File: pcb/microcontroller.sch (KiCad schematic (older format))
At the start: 14 parts, among them J1 JSTA-4, P2 SWD, SW1 SPST, U2 STM32F072CBT6

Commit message: Generated net list (only two footprints remaining), added a few footprints, started rough estimate of PCB size
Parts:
- D401: renamed from D2; footprint (none) -> Woodchuck:CREE_RGB_LED; Farnell (none) -> 2093940
- gave numbers to parts that had none: 1
- renumbered C5 to C401, C6 to C402, C7 to C403, C8 to C404, J1 to J401, P2 to P401, R2 to R401, R3 to R402, R4 to R403, R1 to R404, SW1 to SW401, U2 to U401
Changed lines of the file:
@@
 $EndDescr
 $Comp
-L GND #PWR24
+L GND #PWR017
 U 1 1 565B23CF
 P 5900 5600
-F 0 "#PWR24" H 5900 5350 50  0001 C CNN
+F 0 "#PWR017" H 5900 5350 50  0001 C CNN
 F 1 "GND" H 5900 5450 50  0000 C CNN
 F 2 "" H 5900 5600 60  0000 C CNN
@@
 $EndComp
 $Comp
-L C C7
+L C C403
 U 1 1 565B2484
 P 3000 2000
-F 0 "C7" H 3025 2100 50  0000 L CNN
+F 0 "C403" H 3025 2100 50  0000 L CNN
 F 1 "0.1uF" H 3025 1900 50  0000 L CNN
 F 2 "Woodchuck:C0603" H 3038 1850 30  0000 C CNN
@@
 $EndComp
 $Comp
-L GND #PWR21
+L GND #PWR018
 U 1 1 565B2D06
 P 3000 2350
-F 0 "#PWR21" H 3000 2100 50  0001 C CNN
+F 0 "#PWR018" H 3000 2100 50  0001 C CNN
 F 1 "GND" H 3000 2200 50  0000 C CNN
 F 2 "" H 3000 2350 60  0000 C CNN
@@
 $EndComp
 $Comp
-L C C6
+L C C402
 U 1 1 565B2D3B
 P 2750 2000
-F 0 "C6" H 2775 2100 50  0000 L CNN
+F 0 "C402" H 2775 2100 50  0000 L CNN
 F 1 "0.1uF" H 2775 1900 50  0000 L CNN
 F 2 "Woodchuck:C0603" H 2788 1850 30  0000 C CNN
@@
 NOTE: Place one near each\nVDD pin (24, 48) and one\nnear VDDIO2 (36)
 $Comp
-L C C5
+L C C401
 U 1 1 565B339D
 P 1650 2000
-F 0 "C5" H 1675 2100 50  0000 L CNN
+F 0 "C401" H 1675 2100 50  0000 L CNN
 F 1 "10nF" H 1675 1900 50  0000 L CNN
 F 2 "Woodchuck:C0603" H 1688 1850 30  0000 C CNN
@@
 $EndComp
 $Comp
-L GND #PWR13
+L GND #PWR019
 U 1 1 565B33AB
 P 1650 2250
-F 0 "#PWR13" H 1650 2000 50  0001 C CNN
+F 0 "#PWR019" H 1650 2000 50  0001 C CNN
 F 1 "GND" H 1650 2100 50  0000 C CNN
 F 2 "" H 1650 2250 60  0000 C CNN
@@
 NOTE: Place near VDDA (9)
 $Comp
-L C C8
+L C C404
 U 1 1 565B3429
 P 3250 2000
-F 0 "C8" H 3275 2100 50  0000 L CNN
+F 0 "C404" H 3275 2100 50  0000 L CNN
 F 1 "0.1uF" H 3275 1900 50  0000 L CNN
 F 2 "Woodchuck:C0603" H 3288 1850 30  0000 C CNN
@@
 NOTE: VDD supply needs 4.7uF across it
 $Comp
-L SWD P2
+L SWD P401
 U 1 1 565B3F04
 P 2300 3450
-F 0 "P2" H 2550 3750 60  0000 C CNN
+F 0 "P401" H 2550 3750 60  0000 C CNN
 F 1 "SWD" H 2000 3750 60  0000 C CNN
 F 2 "Woodchuck:FTSH-105-01-F-D-K" H 2650 3250 60  0001 C CNN
@@
 SWCLK
 $Comp
-L GND #PWR15
+L GND #PWR020
 U 1 1 565B4620
 P 1700 3750
-F 0 "#PWR15" H 1700 3500 50  0001 C CNN
+F 0 "#PWR020" H 1700 3500 50  0001 C CNN
 F 1 "GND" H 1700 3600 50  0000 C CNN
 F 2 "" H 1700 3750 60  0000 C CNN
@@
 $EndComp
 $Comp
-L JSTA-4 J1
+L JSTA-4 J401
 U 1 1 565B5A63
 P 2500 4550
-F 0 "J1" H 2550 4100 60  0000 C CNN
+F 0 "J401" H 2550 4100 60  0000 C CNN
 F 1 "JSTA-4" H 2500 4600 60  0000 C CNN
 F 2 "Woodchuck:S04B-PASK-2" H 2500 4650 60  0001 C CNN
@@
 EXT_RX
 $Comp
-L GND #PWR17
+L GND #PWR021
 U 1 1 565B6C28
 P 2200 5000
-F 0 "#PWR17" H 2200 4750 50  0001 C CNN
+F 0 "#PWR021" H 2200 4750 50  0001 C CNN
 F 1 "GND" H 2200 4850 50  0000 C CNN
 F 2 "" H 2200 5000 60  0000 C CNN
@@
 EXT PORT
 $Comp
-L GND #PWR18
+L GND #PWR022
 U 1 1 565B80EF
 P 2400 6100
-F 0 "#PWR18" H 2400 5850 50  0001 C CNN
+F 0 "#PWR022" H 2400 5850 50  0001 C CNN
 F 1 "GND" H 2400 5950 50  0000 C CNN
 F 2 "" H 2400 6100 60  0000 C CNN
@@
 $EndComp
 $Comp
-L GND #PWR19
+L GND #PWR023
 U 1 1 565B8112
 P 2800 6300
-F 0 "#PWR19" H 2800 6050 50  0001 C CNN
+F 0 "#PWR023" H 2800 6050 50  0001 C CNN
 F 1 "GND" H 2800 6150 50  0000 C CNN
 F 2 "" H 2800 6300 60  0000 C CNN
@@
 BOOT0
 $Comp
-L SPST SW1
+L SPST SW401
 U 1 1 565B9D59
 P 8550 4750
-F 0 "SW1" H 8550 4850 50  0000 C CNN
+F 0 "SW401" H 8550 4850 50  0000 C CNN
 F 1 "SPST" H 8550 4650 50  0000 C CNN
 F 2 "" H 8550 4750 60  0000 C CNN
@@
 BOOT0
 $Comp
-L RESISTOR R1
+L RESISTOR R404
 U 1 1 565BA71B
 P 7950 5100
-F 0 "R1" H 8070 5190 60  0000 C CNN
+F 0 "R404" H 8070 5190 60  0000 C CNN
 F 1 "10K" H 7950 4950 60  0000 C CNN
 F 2 "Woodchuck:0603" H 7950 4850 60  0000 C CNN
@@
 $EndComp
 $Comp
-L GND #PWR25
+L GND #PWR024
 U 1 1 565BAC22
 P 7950 5450
-F 0 "#PWR25" H 7950 5200 50  0001 C CNN
+F 0 "#PWR024" H 7950 5200 50  0001 C CNN
 F 1 "GND" H 7950 5300 50  0000 C CNN
 F 2 "" H 7950 5450 60  0000 C CNN
@@
 BOOTLOADER SELECT
 $Comp
-L +3.3V #PWR26
+L +3.3V #PWR025
 U 1 1 565F343F
 P 9150 4650
-F 0 "#PWR26" H 9150 4500 50  0001 C CNN
+F 0 "#PWR025" H 9150 4500 50  0001 C CNN
 F 1 "+3.3V" H 9150 4790 50  0000 C CNN
 F 2 "" H 9150 4650 50  0000 C CNN
@@
 $EndComp
 $Comp
-L +3.3V #PWR16
+L +3.3V #PWR026
 U 1 1 565F3C95
 P 2200 4500
-F 0 "#PWR16" H 2200 4350 50  0001 C CNN
+F 0 "#PWR026" H 2200 4350 50  0001 C CNN
 F 1 "+3.3V" H 2200 4640 50  0000 C CNN
 F 2 "" H 2200 4500 50  0000 C CNN
@@
 $EndComp
 $Comp
-L +3.3V #PWR14
+L +3.3V #PWR027
 U 1 1 565F3F3F
 P 1700 3150
-F 0 "#PWR14" H 1700 3000 50  0001 C CNN
+F 0 "#PWR027" H 1700 3000 50  0001 C CNN
 F 1 "+3.3V" H 1700 3290 50  0000 C CNN
 F 2 "" H 1700 3150 50  0000 C CNN
@@
 $EndComp
 $Comp
-L +3.3V #PWR20
+L +3.3V #PWR028
 U 1 1 565F40A9
 P 3000 1650
-F 0 "#PWR20" H 3000 1500 50  0001 C CNN
+F 0 "#PWR028" H 3000 1500 50  0001 C CNN
 F 1 "+3.3V" H 3000 1790 50  0000 C CNN
 F 2 "" H 3000 1650 50  0000 C CNN
@@
 $EndComp
 $Comp
-L +3.3V #PWR12
+L +3.3V #PWR029
 U 1 1 565F40DC
 P 1650 1750
-F 0 "#PWR12" H 1650 1600 50  0001 C CNN
+F 0 "#PWR029" H 1650 1600 50  0001 C CNN
 F 1 "+3.3V" H 1650 1890 50  0000 C CNN
 F 2 "" H 1650 1750 50  0000 C CNN
@@
 $EndComp
 $Comp
-L +3.3V #PWR23
+L +3.3V #PWR030
 U 1 1 565F4A36
 P 5800 2400
-F 0 "#PWR23" H 5800 2250 50  0001 C CNN
+F 0 "#PWR030" H 5800 2250 50  0001 C CNN
 F 1 "+3.3V" H 5800 2540 50  0000 C CNN
 F 2 "" H 5800 2400 50  0000 C CNN
@@
 NoConn ~ 5500 2600
 $Comp
-L LED_RCBG D2
+L LED_RCBG D401
 U 1 1 569D292A
 P 3700 4500
-F 0 "D2" H 3700 4850 50  0000 C CNN
+F 0 "D401" H 3700 4850 50  0000 C CNN
 F 1 "LED_RCBG" H 3700 4150 50  0000 C CNN
-F 2 "" H 3700 4450 50  0000 C CNN
-F 3 "" H 3700 4450 50  0000 C CNN
+F 2 "Woodchuck:CREE_RGB_LED" H 3650 5000 50  0000 C CNN
+F 3 "http://www.farnell.com/datasheets/1965387.pdf" H 3600 4900 50  0000 C CNN
+F 4 "2093940" H 3700 4500 60  0001 C CNN "Farnell"
 	1    3700 4500
 	0    -1   -1   0
 $EndComp
 $Comp
-L RESISTOR R2
+L RESISTOR R401
 U 1 1 569D2BC0
 P 4500 4000
-F 0 "R2" H 4620 4090 60  0000 C CNN
+F 0 "R401" H 4620 4090 60  0000 C CNN
 F 1 "RESISTOR" H 4500 3850 60  0001 C CNN
 F 2 "Woodchuck:0603" H 4500 4000 60  0001 C CNN
@@
 $EndComp
 $Comp
-L RESISTOR R3
+L RESISTOR R402
 U 1 1 569D2C37
 P 4500 4100
-F 0 "R3" H 4620 4190 60  0000 C CNN
+F 0 "R402" H 4620 4190 60  0000 C CNN
 F 1 "RESISTOR" H 4500 3950 60  0001 C CNN
 F 2 "Woodchuck:0603" H 4500 4100 60  0001 C CNN
@@
 $EndComp
 $Comp
-L RESISTOR R4
+L RESISTOR R403
 U 1 1 569D2C6E
 P 4500 4200
-F 0 "R4" H 4620 4290 60  0000 C CNN
+F 0 "R403" H 4620 4290 60  0000 C CNN
 F 1 "RESISTOR" H 4500 4050 60  0001 C CNN
 F 2 "Woodchuck:0603" H 4500 4200 60  0001 C CNN
@@
 $EndComp
 $Comp
-L STM32F072CBT6 U2
+L STM32F072CBT6 U401
 U 1 1 565B237E
 P 5050 2800
-F 0 "U2" H 5100 2850 60  0000 C CNN
+F 0 "U401" H 5100 2850 60  0000 C CNN
 F 1 "STM32F072CBT6" H 6300 2850 60  0000 C CNN
 F 2 "Woodchuck:LQFP48" H 5400 2900 60  0001 C CNN
@@
 $EndComp
 $Comp
-L GND #PWR22
+L GND #PWR031
 U 1 1 569D2FC5
 P 3700 4850
-F 0 "#PWR22" H 3700 4600 50  0001 C CNN
+F 0 "#PWR031" H 3700 4600 50  0001 C CNN
 F 1 "GND" H 3700 4700 50  0000 C CNN
 F 2 "" H 3700 4850 60  0000 C CNN
@@
 $EndComp
 $Comp
-L USB_OTG P?
+L USB_OTG P402
 U 1 1 569D56C3
 P 2700 5850
-F 0 "P?" H 3025 5725 50  0000 C CNN
+F 0 "P402" H 3025 5725 50  0000 C CNN
 F 1 "USB_OTG" H 2700 6050 50  0000 C CNN
 F 2 "Woodchuck:MOLEX_67503_1020_MINI_USB" V 2650 5750 60  0001 C CNN

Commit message: Fix LED circuit and radio tx/rx labels, start LED driver code
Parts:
- D401: value LED_RCBG -> LED_RABG; symbol LED_RCBG -> LED_RABG; Digikey (none) -> Value; Fieldname (none) -> Value
- R401, R402, R403: value RESISTOR -> 510; Farnell Value -> 1469826
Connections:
- wire segments 69 -> 70
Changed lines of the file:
@@
 NoConn ~ 5500 2600
 $Comp
-L LED_RCBG D401
+L LED_RABG D401
 U 1 1 569D292A
-P 3700 4500
-F 0 "D401" H 3700 4850 50  0000 C CNN
-F 1 "LED_RCBG" H 3700 4150 50  0000 C CNN
-F 2 "Woodchuck:CREE_RGB_LED" H 3650 5000 50  0000 C CNN
-F 3 "http://www.farnell.com/datasheets/1965387.pdf" H 3600 4900 50  0000 C CNN
-F 4 "2093940" H 3700 4500 60  0001 C CNN "Farnell"
-	1    3700 4500
+P 3700 3550
+F 0 "D401" H 3700 3900 50  0000 C CNN
+F 1 "LED_RABG" H 3700 3200 50  0001 C CNN
+F 2 "Woodchuck:CREE_RGB_LED" H 3650 4050 50  0001 C CNN
+F 3 "http://www.farnell.com/datasheets/1965387.pdf" H 3600 3950 50  0001 C CNN
+F 4 "Value" H 3700 3550 60  0001 C CNN "Digikey"
+F 5 "2093940" H 3700 3550 60  0001 C CNN "Farnell"
+F 6 "Value" H 3700 3550 60  0001 C CNN "Fieldname"
+	1    3700 3550
 	0    -1   -1   0
 $EndComp
@@
 P 4500 4000
 F 0 "R401" H 4620 4090 60  0000 C CNN
-F 1 "RESISTOR" H 4500 3850 60  0001 C CNN
+F 1 "510" H 4500 3850 60  0001 C CNN
 F 2 "Woodchuck:0603" H 4500 4000 60  0001 C CNN
 F 3 "" H 4500 4000 60  0000 C CNN
 F 4 "Value" H 4500 4000 60  0001 C CNN "Digikey"
-F 5 "Value" H 4500 4000 60  0001 C CNN "Farnell"
+F 5 "1469826" H 4500 4000 60  0001 C CNN "Farnell"
 F 6 "Value" H 4500 4000 60  0001 C CNN "Fieldname"
 	1    4500 4000
@@
 P 4500 4100
 F 0 "R402" H 4620 4190 60  0000 C CNN
-F 1 "RESISTOR" H 4500 3950 60  0001 C CNN
+F 1 "510" H 4500 3950 60  0001 C CNN
 F 2 "Woodchuck:0603" H 4500 4100 60  0001 C CNN
 F 3 "" H 4500 4100 60  0000 C CNN
 F 4 "Value" H 4500 4100 60  0001 C CNN "Digikey"
-F 5 "Value" H 4500 4100 60  0001 C CNN "Farnell"
+F 5 "1469826" H 4500 4100 60  0001 C CNN "Farnell"
 F 6 "Value" H 4500 4100 60  0001 C CNN "Fieldname"
 	1    4500 4100
@@
 P 4500 4200
 F 0 "R403" H 4620 4290 60  0000 C CNN
-F 1 "RESISTOR" H 4500 4050 60  0001 C CNN
+F 1 "510" H 4500 4050 60  0001 C CNN
 F 2 "Woodchuck:0603" H 4500 4200 60  0001 C CNN
 F 3 "" H 4500 4200 60  0000 C CNN
 F 4 "Value" H 4500 4200 60  0001 C CNN "Digikey"
-F 5 "Value" H 4500 4200 60  0001 C CNN "Farnell"
+F 5 "1469826" H 4500 4200 60  0001 C CNN "Farnell"
 F 6 "Value" H 4500 4200 60  0001 C CNN "Fieldname"
 	1    4500 4200
@@
 F 6 "Value" H 5050 2800 60  0001 C CNN "Fieldname"
 	1    5050 2800
-	1    0    0    -1
-$EndComp
-$Comp
-L GND #PWR031
-U 1 1 569D2FC5
-P 3700 4850
-F 0 "#PWR031" H 3700 4600 50  0001 C CNN
-F 1 "GND" H 3700 4700 50  0000 C CNN
-F 2 "" H 3700 4850 60  0000 C CNN
-F 3 "" H 3700 4850 60  0000 C CNN
-	1    3700 4850
 	1    0    0    -1
 $EndComp
@@
 Connection ~ 6000 5500
 Wire Wire Line
-	3900 4200 4250 4200
-Wire Wire Line
-	4250 4100 3700 4100
-Wire Wire Line
-	3700 4100 3700 4200
-Wire Wire Line
-	4250 4000 3500 4000
-Wire Wire Line
-	3500 4000 3500 4200
-Wire Wire Line
 	4750 4000 4850 4000
 Wire Wire Line
@@
 Wire Wire Line
 	4750 4200 4850 4200
-Wire Wire Line
-	3700 4850 3700 4800
 Wire Wire Line
 	2400 5750 2200 5750
@@
 Wire Wire Line
 	2800 6250 2800 6300
+Wire Wire Line
+	3900 4000 4250 4000
+Wire Wire Line
+	3900 3850 3900 4000
+Wire Wire Line
+	3700 3850 3700 4100
+Wire Wire Line
+	3700 4100 4250 4100
+Wire Wire Line
+	3500 4200 4250 4200
+Wire Wire Line
+	3500 3850 3500 4200
+$Comp
+L +3.3V #PWR?
+U 1 1 56B44BB2
+P 3700 3300
+F 0 "#PWR?" H 3700 3150 50  0001 C CNN
+F 1 "+3.3V" H 3700 3440 50  0000 C CNN
+F 2 "" H 3700 3300 60  0000 C CNN
+F 3 "" H 3700 3300 60  0000 C CNN
+	1    3700 3300
+	1    0    0    -1
+$EndComp
+Wire Wire Line
+	3700 3350 3700 3300
 $EndSCHEMATC

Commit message: Fix barometer hierarchical pins and add Farnell numbers to components
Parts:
- C401: Farnell Value -> 1907314
- C402, C403, C404: Farnell Value -> 9406140
- J401: Farnell Value -> 1830749
- P401: Farnell Value -> 1865285
- R404: Digikey (none) -> Value; Farnell (none) -> 9331700; Fieldname (none) -> Value
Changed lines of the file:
@@
 $EndDescr
 $Comp
-L GND #PWR017
+L GND #PWR015
 U 1 1 565B23CF
 P 5900 5600
-F 0 "#PWR017" H 5900 5350 50  0001 C CNN
+F 0 "#PWR015" H 5900 5350 50  0001 C CNN
 F 1 "GND" H 5900 5450 50  0000 C CNN
 F 2 "" H 5900 5600 60  0000 C CNN
@@
 F 3 "" H 3000 2000 60  0000 C CNN
 F 4 "Value" H 3000 2000 60  0001 C CNN "Digikey"
-F 5 "Value" H 3000 2000 60  0001 C CNN "Farnell"
+F 5 "9406140" H 3000 2000 60  0001 C CNN "Farnell"
 F 6 "Value" H 3000 2000 60  0001 C CNN "Fieldname"
 	1    3000 2000
@@
 $EndComp
 $Comp
-L GND #PWR018
+L GND #PWR016
 U 1 1 565B2D06
 P 3000 2350
-F 0 "#PWR018" H 3000 2100 50  0001 C CNN
+F 0 "#PWR016" H 3000 2100 50  0001 C CNN
 F 1 "GND" H 3000 2200 50  0000 C CNN
 F 2 "" H 3000 2350 60  0000 C CNN
@@
 F 3 "" H 2750 2000 60  0000 C CNN
 F 4 "Value" H 2750 2000 60  0001 C CNN "Digikey"
-F 5 "Value" H 2750 2000 60  0001 C CNN "Farnell"
+F 5 "9406140" H 2750 2000 60  0001 C CNN "Farnell"
 F 6 "Value" H 2750 2000 60  0001 C CNN "Fieldname"
 	1    2750 2000
@@
 F 3 "" H 1650 2000 60  0000 C CNN
 F 4 "Value" H 1650 2000 60  0001 C CNN "Digikey"
-F 5 "Value" H 1650 2000 60  0001 C CNN "Farnell"
+F 5 "1907314" H 1650 2000 60  0001 C CNN "Farnell"
 F 6 "Value" H 1650 2000 60  0001 C CNN "Fieldname"
 	1    1650 2000
@@
 $EndComp
 $Comp
-L GND #PWR019
+L GND #PWR017
 U 1 1 565B33AB
 P 1650 2250
-F 0 "#PWR019" H 1650 2000 50  0001 C CNN
+F 0 "#PWR017" H 1650 2000 50  0001 C CNN
 F 1 "GND" H 1650 2100 50  0000 C CNN
 F 2 "" H 1650 2250 60  0000 C CNN
@@
 F 3 "" H 3250 2000 60  0000 C CNN
 F 4 "Value" H 3250 2000 60  0001 C CNN "Digikey"
-F 5 "Value" H 3250 2000 60  0001 C CNN "Farnell"
+F 5 "9406140" H 3250 2000 60  0001 C CNN "Farnell"
 F 6 "Value" H 3250 2000 60  0001 C CNN "Fieldname"
 	1    3250 2000
@@
 F 3 "" H 2650 3250 60  0000 C CNN
 F 4 "Value" H 2300 3450 60  0001 C CNN "Digikey"
-F 5 "Value" H 2300 3450 60  0001 C CNN "Farnell"
+F 5 "1865285" H 2300 3450 60  0001 C CNN "Farnell"
 F 6 "Value" H 2300 3450 60  0001 C CNN "Fieldname"
 	1    2300 3450
@@
 SWCLK
 $Comp
-L GND #PWR020
+L GND #PWR018
 U 1 1 565B4620
 P 1700 3750
-F 0 "#PWR020" H 1700 3500 50  0001 C CNN
+F 0 "#PWR018" H 1700 3500 50  0001 C CNN
 F 1 "GND" H 1700 3600 50  0000 C CNN
 F 2 "" H 1700 3750 60  0000 C CNN
@@
 F 3 "" H 2500 4650 60  0000 C CNN
 F 4 "Value" H 2500 4550 60  0001 C CNN "Digikey"
-F 5 "Value" H 2500 4550 60  0001 C CNN "Farnell"
+F 5 "1830749" H 2500 4550 60  0001 C CNN "Farnell"
 F 6 "Value" H 2500 4550 60  0001 C CNN "Fieldname"
 	1    2500 4550
@@
 EXT_RX
 $Comp
-L GND #PWR021
+L GND #PWR019
 U 1 1 565B6C28
 P 2200 5000
-F 0 "#PWR021" H 2200 4750 50  0001 C CNN
+F 0 "#PWR019" H 2200 4750 50  0001 C CNN
 F 1 "GND" H 2200 4850 50  0000 C CNN
 F 2 "" H 2200 5000 60  0000 C CNN
@@
 EXT PORT
 $Comp
-L GND #PWR022
+L GND #PWR020
 U 1 1 565B80EF
 P 2400 6100
-F 0 "#PWR022" H 2400 5850 50  0001 C CNN
+F 0 "#PWR020" H 2400 5850 50  0001 C CNN
 F 1 "GND" H 2400 5950 50  0000 C CNN
 F 2 "" H 2400 6100 60  0000 C CNN
@@
 $EndComp
 $Comp
-L GND #PWR023
+L GND #PWR021
 U 1 1 565B8112
 P 2800 6300
-F 0 "#PWR023" H 2800 6050 50  0001 C CNN
+F 0 "#PWR021" H 2800 6050 50  0001 C CNN
 F 1 "GND" H 2800 6150 50  0000 C CNN
 F 2 "" H 2800 6300 60  0000 C CNN
@@
 F 2 "Woodchuck:0603" H 7950 4850 60  0000 C CNN
 F 3 "" H 7950 5100 60  0000 C CNN
+F 4 "Value" H 7950 5100 60  0001 C CNN "Digikey"
+F 5 "9331700" H 7950 5100 60  0001 C CNN "Farnell"
+F 6 "Value" H 7950 5100 60  0001 C CNN "Fieldname"
 	1    7950 5100
 	0    1    1    0
 $EndComp
 $Comp
-L GND #PWR024
+L GND #PWR022
 U 1 1 565BAC22
 P 7950 5450
-F 0 "#PWR024" H 7950 5200 50  0001 C CNN
+F 0 "#PWR022" H 7950 5200 50  0001 C CNN
 F 1 "GND" H 7950 5300 50  0000 C CNN
 F 2 "" H 7950 5450 60  0000 C CNN
@@
 BOOTLOADER SELECT
 $Comp
-L +3.3V #PWR025
+L +3.3V #PWR023
 U 1 1 565F343F
 P 9150 4650
-F 0 "#PWR025" H 9150 4500 50  0001 C CNN
+F 0 "#PWR023" H 9150 4500 50  0001 C CNN
 F 1 "+3.3V" H 9150 4790 50  0000 C CNN
 F 2 "" H 9150 4650 50  0000 C CNN
@@
 $EndComp
 $Comp
-L +3.3V #PWR026
+L +3.3V #PWR024
 U 1 1 565F3C95
 P 2200 4500
-F 0 "#PWR026" H 2200 4350 50  0001 C CNN
+F 0 "#PWR024" H 2200 4350 50  0001 C CNN
 F 1 "+3.3V" H 2200 4640 50  0000 C CNN
 F 2 "" H 2200 4500 50  0000 C CNN
@@
 $EndComp
 $Comp
-L +3.3V #PWR027
+L +3.3V #PWR025
 U 1 1 565F3F3F
 P 1700 3150
-F 0 "#PWR027" H 1700 3000 50  0001 C CNN
+F 0 "#PWR025" H 1700 3000 50  0001 C CNN
 F 1 "+3.3V" H 1700 3290 50  0000 C CNN
 F 2 "" H 1700 3150 50  0000 C CNN
@@
 $EndComp
 $Comp
-L +3.3V #PWR028
+L +3.3V #PWR026
 U 1 1 565F40A9
 P 3000 1650
-F 0 "#PWR028" H 3000 1500 50  0001 C CNN
+F 0 "#PWR026" H 3000 1500 50  0001 C CNN
 F 1 "+3.3V" H 3000 1790 50  0000 C CNN
 F 2 "" H 3000 1650 50  0000 C CNN
@@
 $EndComp
 $Comp
-L +3.3V #PWR029
+L +3.3V #PWR027
 U 1 1 565F40DC
 P 1650 1750
-F 0 "#PWR029" H 1650 1600 50  0001 C CNN
+F 0 "#PWR027" H 1650 1600 50  0001 C CNN
 F 1 "+3.3V" H 1650 1890 50  0000 C CNN
 F 2 "" H 1650 1750 50  0000 C CNN
@@
 $EndComp
 $Comp
-L +3.3V #PWR030
+L +3.3V #PWR028
 U 1 1 565F4A36
 P 5800 2400
-F 0 "#PWR030" H 5800 2250 50  0001 C CNN
+F 0 "#PWR028" H 5800 2250 50  0001 C CNN
 F 1 "+3.3V" H 5800 2540 50  0000 C CNN
 F 2 "" H 5800 2400 50  0000 C CNN
@@
 	3500 3850 3500 4200
 $Comp
-L +3.3V #PWR?
+L +3.3V #PWR029
 U 1 1 56B44BB2
 P 3700 3300
-F 0 "#PWR?" H 3700 3150 50  0001 C CNN
+F 0 "#PWR029" H 3700 3150 50  0001 C CNN
 F 1 "+3.3V" H 3700 3440 50  0000 C CNN
 F 2 "" H 3700 3300 60  0000 C CNN

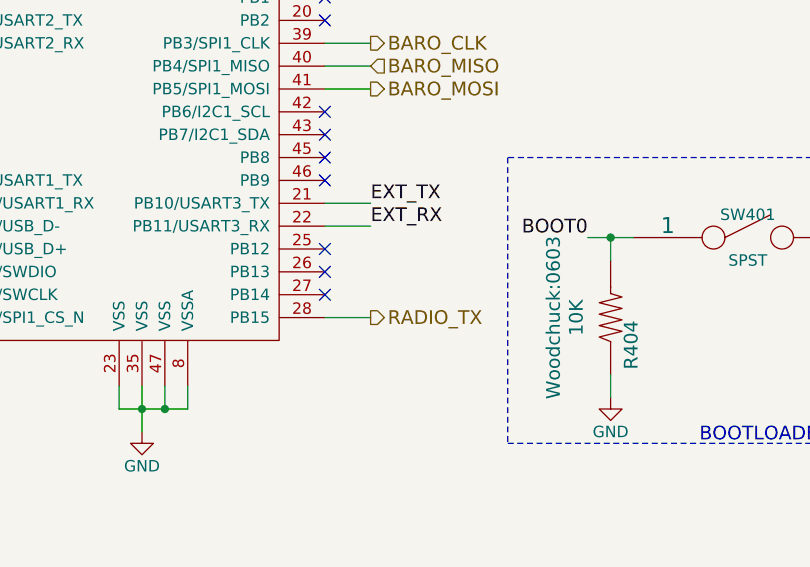
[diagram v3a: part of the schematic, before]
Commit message: Connect MTX2 parallel channel select pins to the MCU
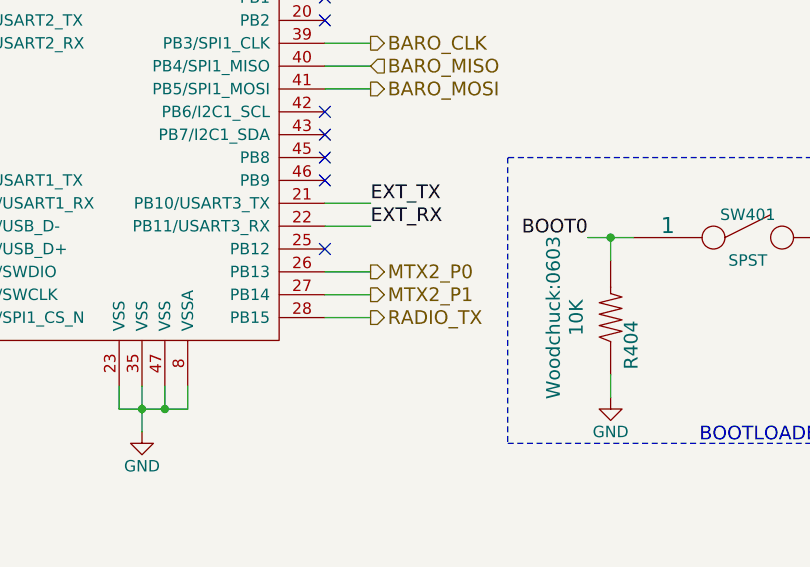
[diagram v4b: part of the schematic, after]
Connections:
- net MTX2_P0: now reaches U401.26 (PB13)
- net MTX2_P1: now reaches U401.27 (PB14)
- no-connect marks 25 -> 23
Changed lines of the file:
@@
 NoConn ~ 6700 4500
 NoConn ~ 6700 4800
-NoConn ~ 6700 4900
-NoConn ~ 6700 5000
 NoConn ~ 4850 4600
 NoConn ~ 4850 4400
@@
 Wire Wire Line
 	3700 3350 3700 3300
+Wire Wire Line
+	6700 4900 6900 4900
+Wire Wire Line
+	6700 5000 6900 5000
+Text HLabel 6900 5000 2    60   Output ~ 0
+MTX2_P1
+Text HLabel 6900 4900 2    60   Output ~ 0
+MTX2_P0
 $EndSCHEMATC

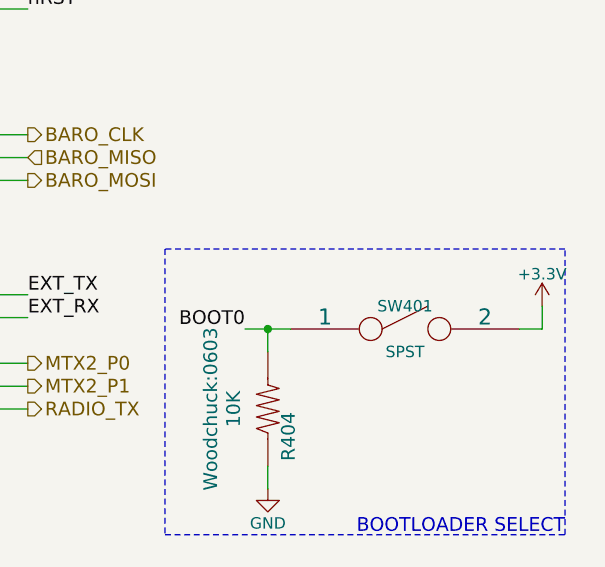
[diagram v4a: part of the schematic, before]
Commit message: Added a missing footprint.
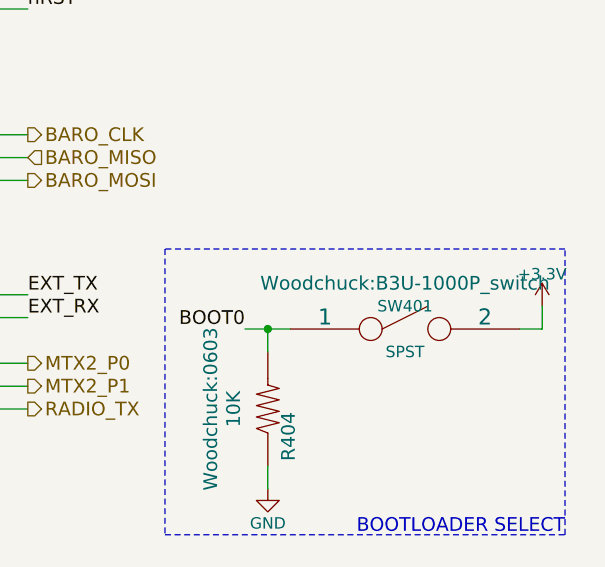
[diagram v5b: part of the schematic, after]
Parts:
- SW401: footprint (none) -> Woodchuck:B3U-1000P_switch
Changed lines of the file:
@@
 F 0 "SW401" H 8550 4850 50  0000 C CNN
 F 1 "SPST" H 8550 4650 50  0000 C CNN
-F 2 "" H 8550 4750 60  0000 C CNN
+F 2 "Woodchuck:B3U-1000P_switch" H 8550 4950 60  0000 C CNN
 F 3 "" H 8550 4750 60  0000 C CNN
 	1    8550 4750
